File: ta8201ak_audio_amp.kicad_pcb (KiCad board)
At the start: 2 copper layers, 39.4 x 34.2 mm, 22 parts, among them J2 IN, J3 AudioGnd, J4 Vcc, J5 RV1_3, J6 RV1_2, J7 Gnd, J8 Out1, J9 Out2

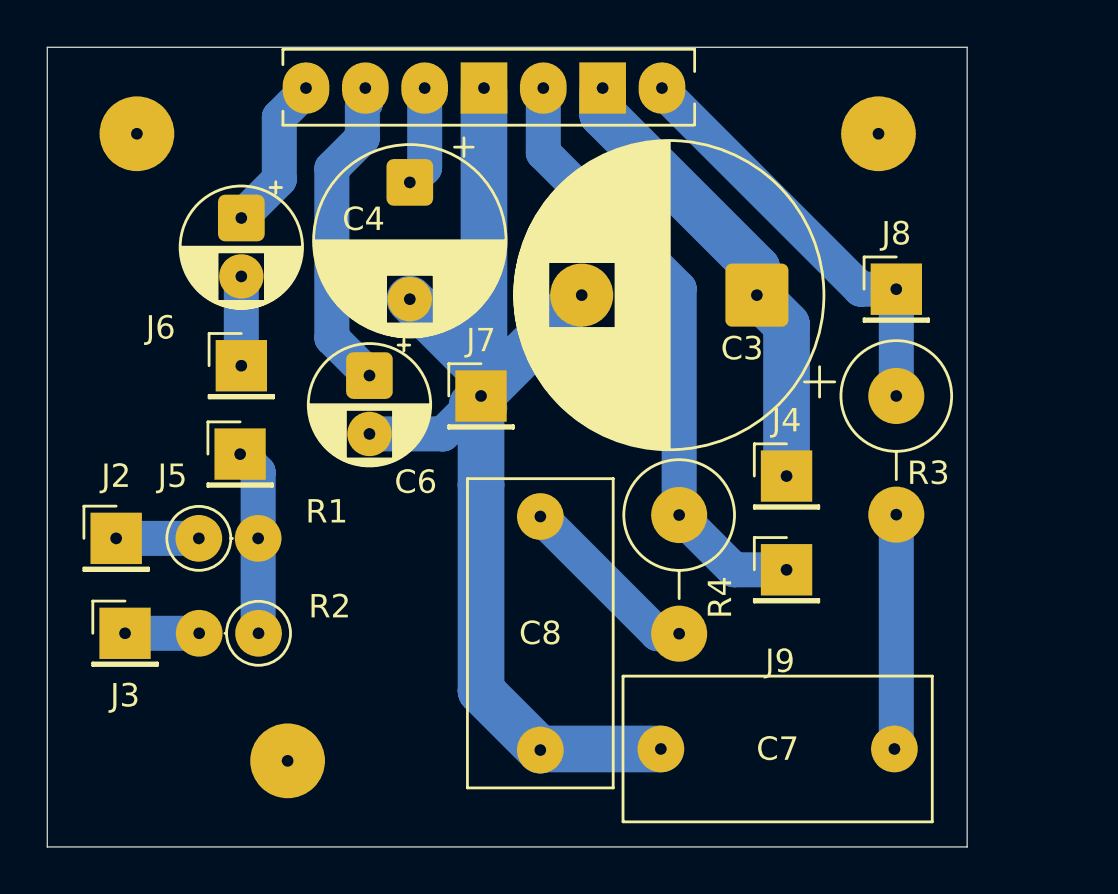
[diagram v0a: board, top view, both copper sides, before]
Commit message: 配線の太さ、パッドの大きさを大きくした
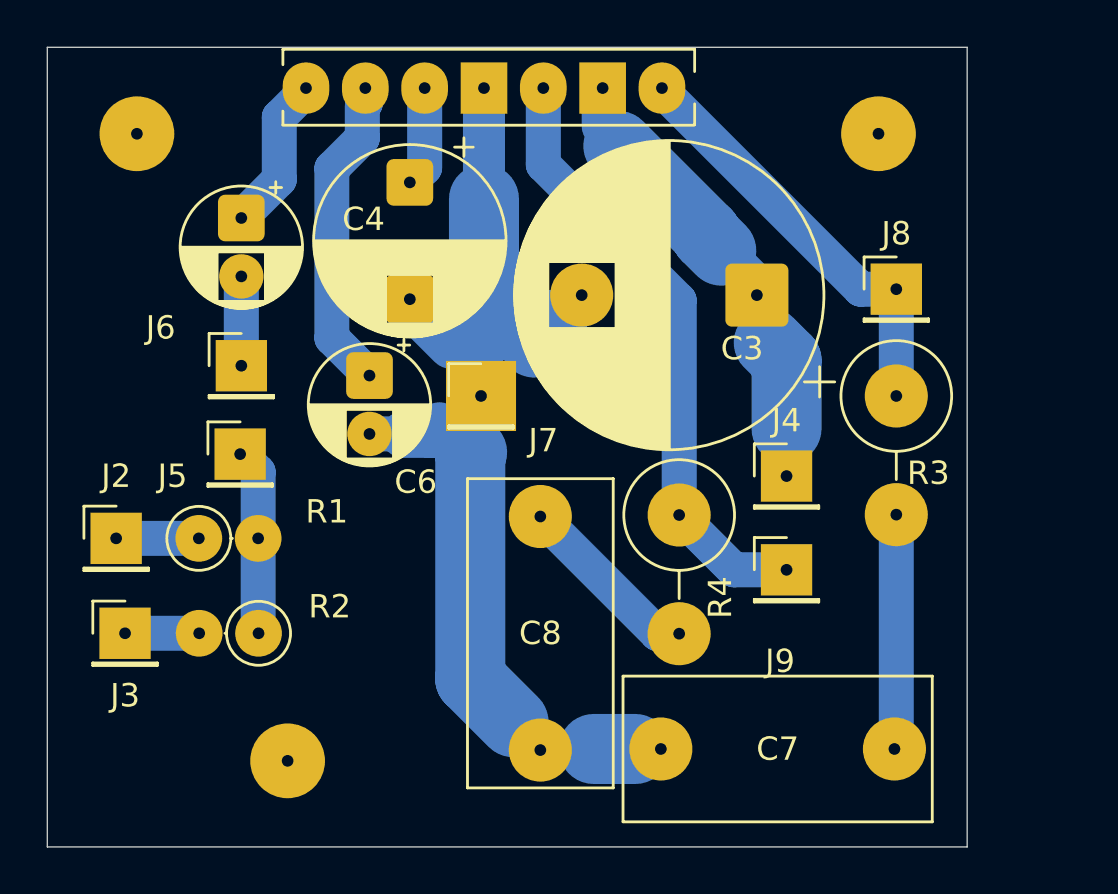
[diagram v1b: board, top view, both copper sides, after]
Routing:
- net GND: track 50.8 -> 36.9 mm
- net VCC: track 20.4 -> 17.2 mm

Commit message: ハムノイズ対策に抵抗を追加してGNDの取り方を変更
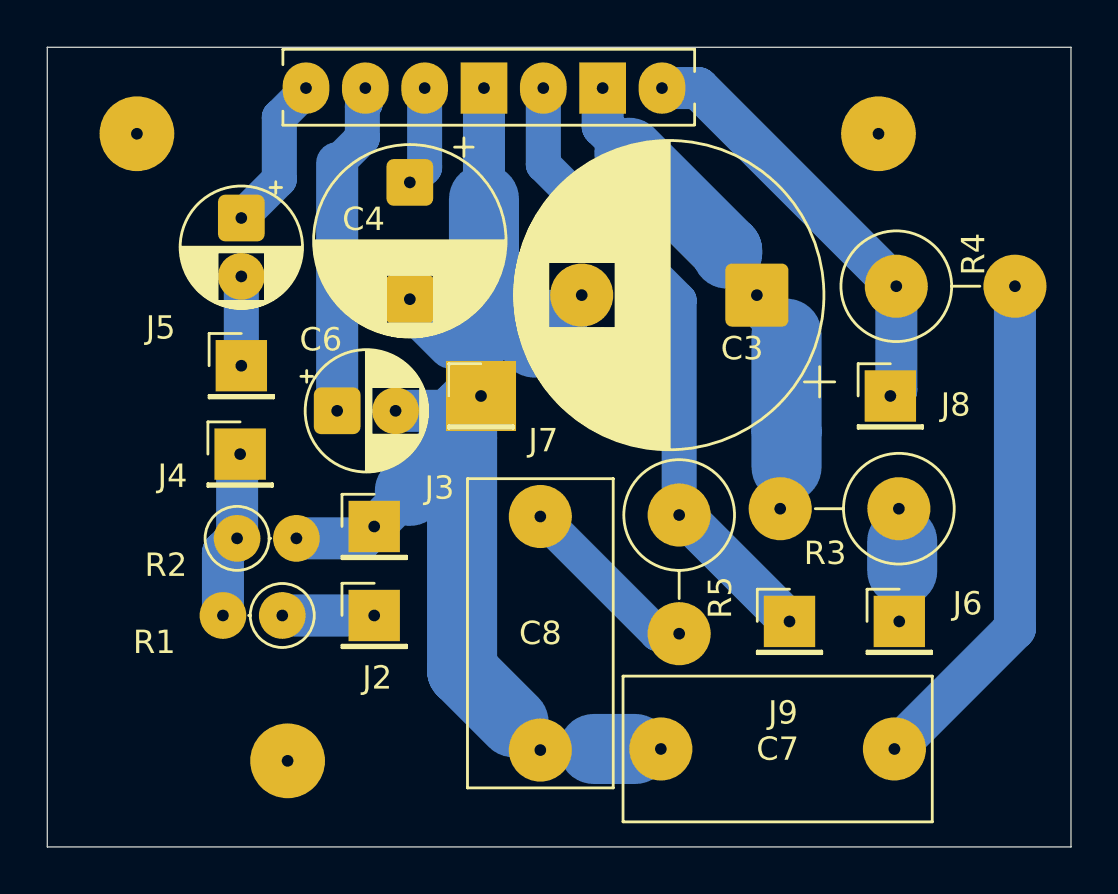
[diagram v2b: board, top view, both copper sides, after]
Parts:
- added R3: 2.2Ω, Resistor_THT:R_Axial_DIN0414_L11.9mm_D4.5mm_P5.08mm_Vertical, F.Cu at (189.8, 72.9)
- C3: value 1000u -> 1000uF
- J3: value AudioGnd -> GND
- moved J3 11.6 mm to (167.4, 73.7)
- moved J2 11.5 mm to (167.4, 77.5)
- moved J6 7.88 mm to (189.9, 77.7)
- moved R1 4.86 mm to (163.4, 77.5), turned to 180 degrees
- moved R4 4.70 mm to (189.7, 63.4), turned to 0 degrees
- moved J8 4.58 mm to (189.5, 68.1)
- moved R2 4.17 mm to (161.5, 74.2), turned to 0 degrees
- moved J9 2.21 mm to (185.2, 77.7)
- moved C6 2.05 mm to (165.8, 68.7), turned to 0 degrees
- renumbered J5 to J4, J6 to J5, J4 to J6, R3 to R4, R4 to R5
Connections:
- C3 pad 1: VCC -> Net-(U1-VCC)
- J3 pad 1: GND2 -> GND
- R2 pad 2: GND2 -> GND
- U1 pad 6: VCC -> Net-(U1-VCC)
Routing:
- net Net-(U1-VCC): track 0.00 -> 17.2 mm
- net VCC: track 17.2 -> 2.75 mm
- net GND: track 36.9 -> 49.4 mm
- net Net-(C7-Pad1): track 10.1 -> 22.1 mm
- net GND2: track 3.18 -> 0.00 mm
- net Net-(J9-Pin_1): track 26.6 -> 27.7 mm
- net Net-(J4-Pin_1): track 8.00 -> 7.21 mm
- net Net-(U1-NF): track 13.5 -> 14.2 mm
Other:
- board size 39.4 x 34.2 mm -> 43.8 x 34.2 mm
